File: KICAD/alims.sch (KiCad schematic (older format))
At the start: 20 parts

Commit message: minor cleanup
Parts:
- gave numbers to parts that had none: 2
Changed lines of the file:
@@
 $Descr A4 11693 8268
 encoding utf-8
-Sheet 13 16
+Sheet 16 16
 Title "SESAME"
 Date ""
@@
 $EndComp
 $Comp
-L Sesame:LT8365 U?
+L Sesame:LT8365 U14
 U 1 1 6123C49A
 P 4850 3400
-F 0 "U?" H 3650 3700 100 0000 L CNN
+F 0 "U14" H 3650 3700 100 0000 L CNN
 F 1 "LT8365" H 3500 3550 100 0000 L CNN
 F 2 "" H 4850 4100 100 0001 C CNN
@@
 AR Path="/60F171CE/6161C7FC" Ref="U?"  Part="3"
 AR Path="/60F19D5B/6161C7FC" Ref="U?"  Part="3"
-AR Path="/60F1AA92/6161C7FC" Ref="U?"  Part="3"
-F 0 "U?" H 963 6904 50  0000 R CNN
+AR Path="/60F1AA92/6161C7FC" Ref="U15"  Part="3"
+F 0 "U15" H 963 6904 50  0000 R CNN
 F 1 "AD8030" H 963 6995 50  0000 R CNN
 F 2 "Package_SO:SO-8_3.9x4.9mm_P1.27mm" H 1150 6950 50  0001 C CNN
@@
 $EndComp
 $Comp
-L Sesame:AD8030 U?
+L Sesame:AD8030 U15
 U 2 1 61592FA9
 P 10200 4550
-F 0 "U?" H 10200 4917 50  0000 C CNN
+F 0 "U15" H 10200 4917 50  0000 C CNN
 F 1 "AD8030" H 10200 4826 50  0000 C CNN
 F 2 "Package_SO:SO-8_3.9x4.9mm_P1.27mm" H 10200 4550 50  0001 C CNN
@@
 $EndComp
 $Comp
-L Sesame:AD8030 U?
+L Sesame:AD8030 U15
 U 1 1 615918A8
 P 9050 2900
-F 0 "U?" H 9050 3267 50  0000 C CNN
+F 0 "U15" H 9050 3267 50  0000 C CNN
 F 1 "AD8030" H 9050 3176 50  0000 C CNN
 F 2 "Package_SO:SO-8_3.9x4.9mm_P1.27mm" H 9050 2900 50  0001 C CNN

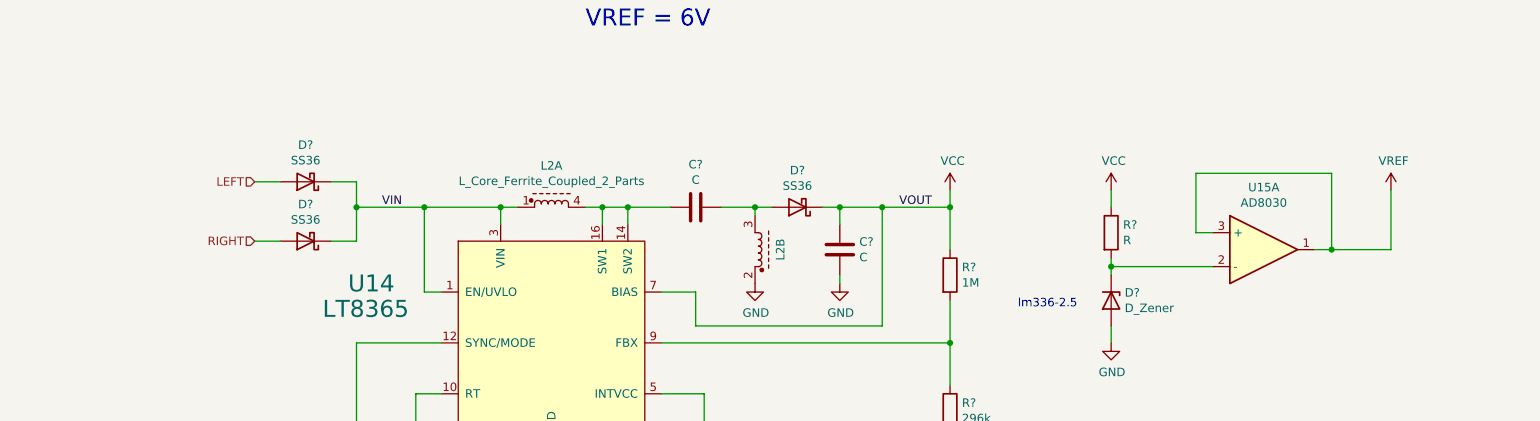
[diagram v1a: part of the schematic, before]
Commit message: drivers draft + clean and minors changes
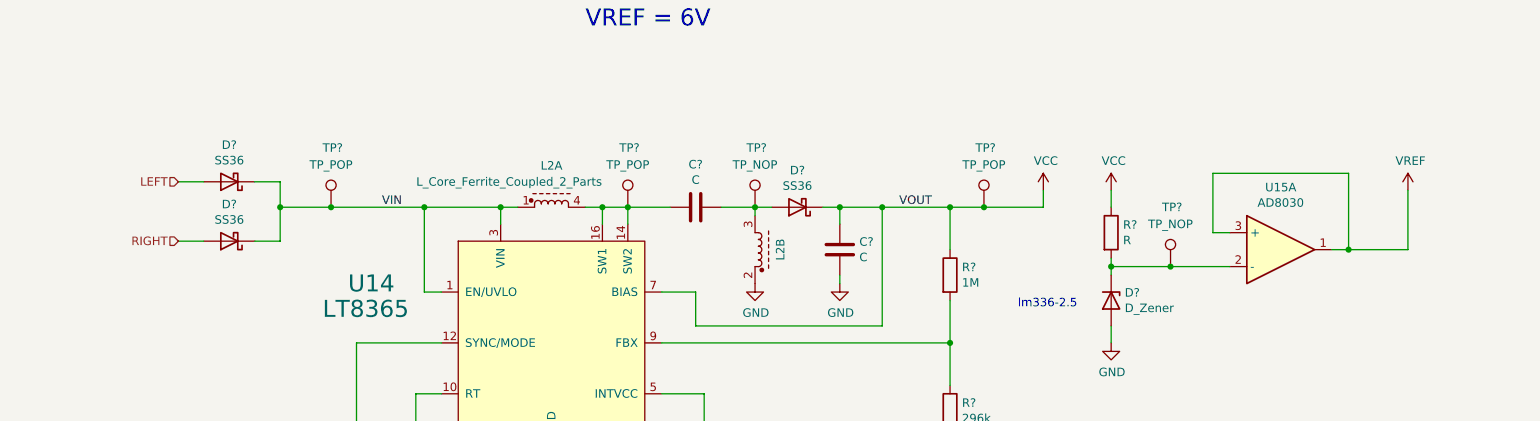
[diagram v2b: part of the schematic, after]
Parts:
- added TP? (x3): TP_POP, symbol Connector:TestPoint
- added TP? (x2): TP_NOP, symbol Connector:TestPoint
- R? (x3): footprint (none) -> Resistor_SMD:R_0805_2012Metric_Pad1.15x1.40mm_HandSolder
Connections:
- net VCC: now also TP?.1
- net VIN: now also TP?.1
- net at D?.1 (K), R?.2, U15.2 (-): now also TP?.1
- net at C?.2, L2.4 (3), U14.14 (SW2)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: now also TP?.1
- net at C?.1, D?.2 (A), L2.3: now also TP?.1
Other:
- moved on the sheet: D?, U15A
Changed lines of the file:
@@
 Comment4 ""
 $EndDescr
-Text HLabel 3100 2500 0    50   Input ~ 0
+Text HLabel 2650 2500 0    50   Input ~ 0
 LEFT
-Text HLabel 3100 2850 0    50   Input ~ 0
+Text HLabel 2650 2850 0    50   Input ~ 0
 RIGHT
 Wire Wire Line
-	8750 2800 8650 2800
-Wire Wire Line
-	9450 2900 9350 2900
+	8850 2800 8750 2800
+Wire Wire Line
+	9550 2900 9450 2900
 $Comp
 L power:GND #PWR0106
@@
 	8150 2950 8150 3000
 Wire Wire Line
-	8150 3000 8750 3000
+	8150 3000 8500 3000
 Connection ~ 8150 3000
 Wire Wire Line
 	8150 3000 8150 3050
 Wire Wire Line
+	2650 2850 2800 2850
+Wire Wire Line
+	2800 2500 2650 2500
+Wire Wire Line
+	3250 2850 3250 2650
+Wire Wire Line
 	3100 2850 3250 2850
 Wire Wire Line
-	3250 2500 3100 2500
-Wire Wire Line
-	3700 2850 3700 2650
-Wire Wire Line
-	3550 2850 3700 2850
-Wire Wire Line
-	3550 2500 3700 2500
+	3100 2500 3250 2500
 $Comp
 L Device:R R?
@@
 $EndComp
 Wire Wire Line
-	8650 2450 9450 2450
-Wire Wire Line
-	8650 2450 8650 2800
-Wire Wire Line
-	9450 2450 9450 2900
+	8750 2450 9550 2450
+Wire Wire Line
+	8750 2450 8750 2800
+Wire Wire Line
+	9550 2450 9550 2900
 $Comp
 L power:VCC #PWR0178
@@
 P 4850 2650
 F 0 "L2" H 4850 2895 50  0000 C CNN
-F 1 "L_Core_Ferrite_Coupled_2_Parts" H 4850 2804 50  0000 C CNN
+F 1 "L_Core_Ferrite_Coupled_2_Parts" H 4600 2800 50  0000 C CNN
 F 2 "" H 4850 2750 50  0001 C CNN
 F 3 "~" H 4850 2750 50  0001 C CNN
@@
 F 0 "R?" H 7270 3096 50  0000 L CNN
 F 1 "1M" H 7270 3005 50  0000 L CNN
-F 2 "" V 7130 3050 50  0001 C CNN
+F 2 "Resistor_SMD:R_0805_2012Metric_Pad1.15x1.40mm_HandSolder" V 7130 3050 50  0001 C CNN
 F 3 "~" H 7200 3050 50  0001 C CNN
 	1    7200 3050
@@
 F 0 "R?" H 7270 3896 50  0000 L CNN
 F 1 "296k" H 7270 3805 50  0000 L CNN
-F 2 "" V 7130 3850 50  0001 C CNN
+F 2 "Resistor_SMD:R_0805_2012Metric_Pad1.15x1.40mm_HandSolder" V 7130 3850 50  0001 C CNN
 F 3 "~" H 7200 3850 50  0001 C CNN
 	1    7200 3850
@@
 F 0 "R?" H 4120 4546 50  0000 L CNN
 F 1 "84.5" H 4120 4455 50  0000 L CNN
-F 2 "" V 3980 4500 50  0001 C CNN
+F 2 "Resistor_SMD:R_0805_2012Metric_Pad1.15x1.40mm_HandSolder" V 3980 4500 50  0001 C CNN
 F 3 "~" H 4050 4500 50  0001 C CNN
 	1    4050 4500
@@
 	5750 4850 5750 4650
 Wire Wire Line
-	4100 2650 3700 2650
+	4100 2650 3550 2650
 Connection ~ 4100 2650
-Connection ~ 3700 2650
-Wire Wire Line
-	3700 2650 3700 2500
+Connection ~ 3250 2650
+Wire Wire Line
+	3250 2650 3250 2500
 Text Label 3850 2650 0    50   ~ 0
 VIN
@@
 L Device:D_Schottky D?
 U 1 1 612B6943
-P 3400 2500
-F 0 "D?" H 3400 2283 50  0000 C CNN
-F 1 "SS36" H 3400 2374 50  0000 C CNN
-F 2 "Diode_SMD:D_SMA_Handsoldering" H 3400 2500 50  0001 C CNN
-F 3 "~" H 3400 2500 50  0001 C CNN
-	1    3400 2500
+P 2950 2500
+F 0 "D?" H 2950 2283 50  0000 C CNN
+F 1 "SS36" H 2950 2374 50  0000 C CNN
+F 2 "Diode_SMD:D_SMA_Handsoldering" H 2950 2500 50  0001 C CNN
+F 3 "~" H 2950 2500 50  0001 C CNN
+	1    2950 2500
 	-1   0    0    1
 $EndComp
@@
 L Device:D_Schottky D?
 U 1 1 612B7084
-P 3400 2850
-F 0 "D?" H 3400 2633 50  0000 C CNN
-F 1 "SS36" H 3400 2724 50  0000 C CNN
-F 2 "Diode_SMD:D_SMA_Handsoldering" H 3400 2850 50  0001 C CNN
-F 3 "~" H 3400 2850 50  0001 C CNN
-	1    3400 2850
+P 2950 2850
+F 0 "D?" H 2950 2633 50  0000 C CNN
+F 1 "SS36" H 2950 2724 50  0000 C CNN
+F 2 "Diode_SMD:D_SMA_Handsoldering" H 2950 2850 50  0001 C CNN
+F 3 "~" H 2950 2850 50  0001 C CNN
+	1    2950 2850
 	-1   0    0    1
 $EndComp
@@
 L power:VCC #PWR?
 U 1 1 612BD8C1
-P 7200 2550
-F 0 "#PWR?" H 7200 2400 50  0001 C CNN
-F 1 "VCC" H 7215 2723 50  0000 C CNN
-F 2 "" H 7200 2550 50  0001 C CNN
-F 3 "" H 7200 2550 50  0001 C CNN
-	1    7200 2550
-	1    0    0    -1
-$EndComp
-Wire Wire Line
-	7200 2550 7200 2650
+P 7750 2550
+F 0 "#PWR?" H 7750 2400 50  0001 C CNN
+F 1 "VCC" H 7765 2723 50  0000 C CNN
+F 2 "" H 7750 2550 50  0001 C CNN
+F 3 "" H 7750 2550 50  0001 C CNN
+	1    7750 2550
+	1    0    0    -1
+$EndComp
 Connection ~ 7200 2650
 $Comp
 L Sesame:VREF #PWR?
 U 1 1 612C58B4
-P 9800 2550
-F 0 "#PWR?" H 9800 2400 50  0001 C CNN
-F 1 "VREF" H 9815 2723 50  0000 C CNN
-F 2 "" H 9800 2550 50  0001 C CNN
-F 3 "" H 9800 2550 50  0001 C CNN
-	1    9800 2550
-	1    0    0    -1
-$EndComp
-Wire Wire Line
-	9800 2550 9800 2900
-Wire Wire Line
-	9800 2900 9450 2900
-Connection ~ 9450 2900
+P 9900 2550
+F 0 "#PWR?" H 9900 2400 50  0001 C CNN
+F 1 "VREF" H 9915 2723 50  0000 C CNN
+F 2 "" H 9900 2550 50  0001 C CNN
+F 3 "" H 9900 2550 50  0001 C CNN
+	1    9900 2550
+	1    0    0    -1
+$EndComp
+Wire Wire Line
+	9900 2550 9900 2900
+Wire Wire Line
+	9900 2900 9550 2900
+Connection ~ 9550 2900
 Text Notes 5050 1600 0    100  ~ 0
 VCC = 7V\nVREF = 6V
@@
 L Sesame:AD8030 U15
 U 1 1 615918A8
-P 9050 2900
-F 0 "U15" H 9050 3267 50  0000 C CNN
-F 1 "AD8030" H 9050 3176 50  0000 C CNN
-F 2 "Package_SO:SO-8_3.9x4.9mm_P1.27mm" H 9050 2900 50  0001 C CNN
-F 3 "~" H 9050 2900 50  0001 C CNN
-	1    9050 2900
-	1    0    0    -1
-$EndComp
+P 9150 2900
+F 0 "U15" H 9150 3267 50  0000 C CNN
+F 1 "AD8030" H 9150 3176 50  0000 C CNN
+F 2 "Package_SO:SO-8_3.9x4.9mm_P1.27mm" H 9150 2900 50  0001 C CNN
+F 3 "~" H 9150 2900 50  0001 C CNN
+	1    9150 2900
+	1    0    0    -1
+$EndComp
+$Comp
+L Connector:TestPoint TP?
+U 1 1 61513B8D
+P 3550 2650
+AR Path="/614794AE/61513B8D" Ref="TP?"  Part="1"
+AR Path="/61456C6A/61513B8D" Ref="TP?"  Part="1"
+AR Path="/61513B8D" Ref="TP?"  Part="1"
+AR Path="/60F1AA92/61513B8D" Ref="TP?"  Part="1"
+F 0 "TP?" H 3500 3000 50  0000 L CNN
+F 1 "TP_POP" H 3550 2900 50  0000 C CNN
+F 2 "" H 3750 2650 50  0001 C CNN
+F 3 "~" H 3750 2650 50  0001 C CNN
+	1    3550 2650
+	1    0    0    -1
+$EndComp
+Connection ~ 3550 2650
+Wire Wire Line
+	3550 2650 3250 2650
+$Comp
+L Connector:TestPoint TP?
+U 1 1 61522F2C
+P 7400 2650
+AR Path="/614794AE/61522F2C" Ref="TP?"  Part="1"
+AR Path="/61456C6A/61522F2C" Ref="TP?"  Part="1"
+AR Path="/61522F2C" Ref="TP?"  Part="1"
+AR Path="/60F1AA92/61522F2C" Ref="TP?"  Part="1"
+F 0 "TP?" H 7350 3000 50  0000 L CNN
+F 1 "TP_POP" H 7400 2900 50  0000 C CNN
+F 2 "" H 7600 2650 50  0001 C CNN
+F 3 "~" H 7600 2650 50  0001 C CNN
+	1    7400 2650
+	1    0    0    -1
+$EndComp
+Wire Wire Line
+	7400 2650 7200 2650
+Wire Wire Line
+	7750 2550 7750 2650
+Wire Wire Line
+	7750 2650 7400 2650
+Connection ~ 7400 2650
+$Comp
+L Connector:TestPoint TP?
+U 1 1 61530DA6
+P 5300 2650
+AR Path="/614794AE/61530DA6" Ref="TP?"  Part="1"
+AR Path="/61456C6A/61530DA6" Ref="TP?"  Part="1"
+AR Path="/61530DA6" Ref="TP?"  Part="1"
+AR Path="/60F1AA92/61530DA6" Ref="TP?"  Part="1"
+F 0 "TP?" H 5250 3000 50  0000 L CNN
+F 1 "TP_POP" H 5300 2900 50  0000 C CNN
+F 2 "" H 5500 2650 50  0001 C CNN
+F 3 "~" H 5500 2650 50  0001 C CNN
+	1    5300 2650
+	1    0    0    -1
+$EndComp
+$Comp
+L Connector:TestPoint TP?
+U 1 1 61533C44
+P 6050 2650
+AR Path="/614794AE/61533C44" Ref="TP?"  Part="1"
+AR Path="/61456C6A/61533C44" Ref="TP?"  Part="1"
+AR Path="/61533C44" Ref="TP?"  Part="1"
+AR Path="/60F1AA92/61533C44" Ref="TP?"  Part="1"
+F 0 "TP?" H 6000 3000 50  0000 L CNN
+F 1 "TP_NOP" H 6050 2900 50  0000 C CNN
+F 2 "" H 6250 2650 50  0001 C CNN
+F 3 "~" H 6250 2650 50  0001 C CNN
+	1    6050 2650
+	1    0    0    -1
+$EndComp
+$Comp
+L Connector:TestPoint TP?
+U 1 1 61535A79
+P 8500 3000
+AR Path="/614794AE/61535A79" Ref="TP?"  Part="1"
+AR Path="/61456C6A/61535A79" Ref="TP?"  Part="1"
+AR Path="/61535A79" Ref="TP?"  Part="1"
+AR Path="/60F1AA92/61535A79" Ref="TP?"  Part="1"
+F 0 "TP?" H 8450 3350 50  0000 L CNN
+F 1 "TP_NOP" H 8500 3250 50  0000 C CNN
+F 2 "" H 8700 3000 50  0001 C CNN
+F 3 "~" H 8700 3000 50  0001 C CNN
+	1    8500 3000
+	1    0    0    -1
+$EndComp
+Connection ~ 8500 3000
+Wire Wire Line
+	8500 3000 8850 3000
 $EndSCHEMATC

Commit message: review w/ jmt
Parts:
- removed D?: D_Zener, symbol Device:D_Zener
- added JP15, JP16: Jumper_2_Bridged, Jumper:SolderJumper-2_P1.3mm_Bridged_Pad1.0x1.5mm, symbol Jumper:Jumper_2_Bridged
- added R84: 10k, symbol Device:R
- added RV4: 10K, Potentiometer_SMD:Potentiometer_Bourns_3214W_Vertical, symbol Device:R_POT
- added TP44: TP_NOP, symbol Connector:TestPoint
- added U16: LM4040DBZ-2.5, Package_TO_SOT_SMD:SOT-23, symbol Reference_Voltage:LM4040DBZ-2.5
- R79, R81, R82: renamed from R?; footprint Resistor_SMD:R_0805_2012Metric_Pad1.15x1.40mm_HandSolder -> (none)
- U14: renamed from U15; footprint Package_SO:SO-8_3.9x4.9mm_P1.27mm -> (none)
- gave numbers to parts that had none: 16
- renumbered L2 to L1, U14 to U15
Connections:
- net GND: now also RV4.3, U16.2 (A)
- net VREF: now also JP15.1 (A), R84.1; no longer U14.3 (+), U14.5 (+)
- net at R83.2, TP43.1: now also U14.3 (+), U16.1 (K); no longer U14.2 (-)
- net at U14.6 (-): now also JP16.1 (A); no longer U14.7
- new net: R84.2, RV4.1, RV4.2, U14.2 (-)
- new net: JP15.2 (B), U14.5 (+)
- new net: JP16.2 (B), TP44.1, U14.7
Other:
- note added: "BOBINE !!!\nCondo serie"
- note added: "REF TENSION AUTRE SOLUTION\n"
- note removed: "lm336-2.5"
- moved on the sheet: D12, D13, R83, TP39, TP43, U14A, U14B

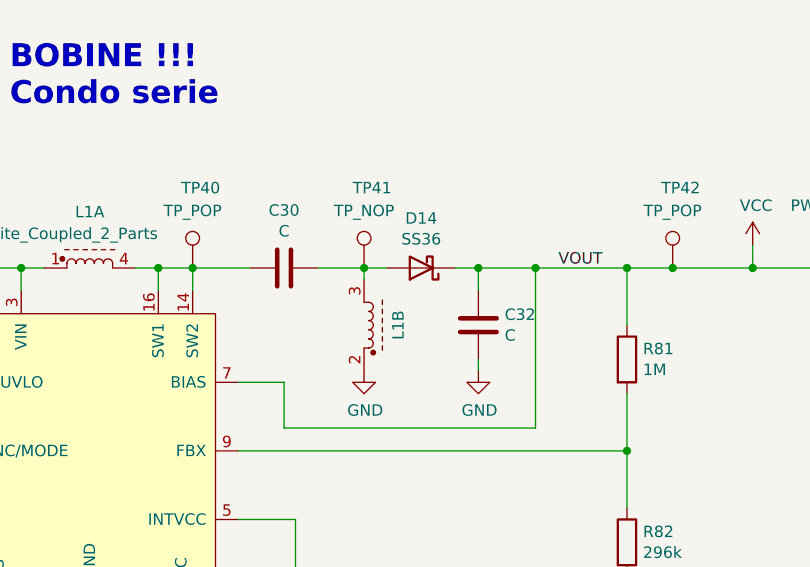
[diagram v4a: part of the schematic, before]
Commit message: edit footprints by jmt
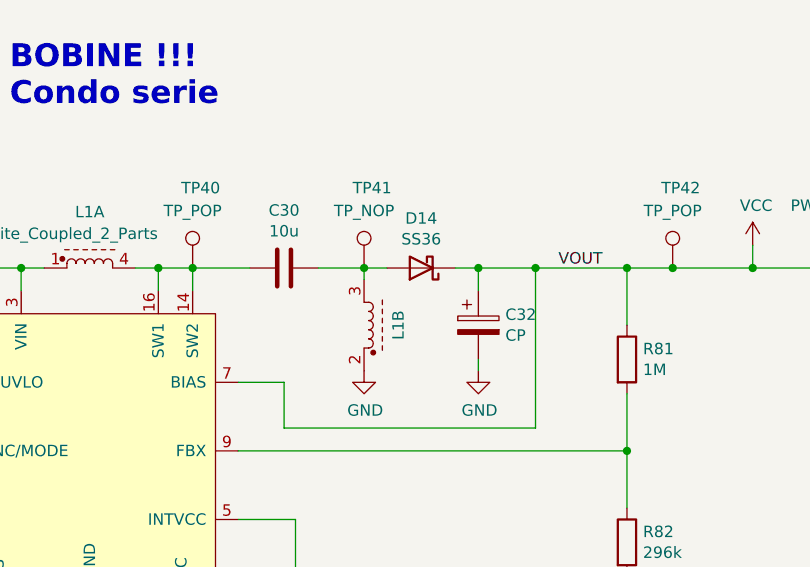
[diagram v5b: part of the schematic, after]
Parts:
- removed C32: C, symbol Device:C
- added C32: CP, symbol Device:CP
- C27, C28, C29, C31: footprint (none) -> Capacitor_SMD:C_0805_2012Metric_Pad1.15x1.40mm_HandSolder
- C30: value C -> 10u; footprint (none) -> Capacitor_SMD:C_1206_3216Metric_Pad1.42x1.75mm_HandSolder
- R79, R80, R81, R82, R83, R84: footprint (none) -> Resistor_SMD:R_0805_2012Metric_Pad1.15x1.40mm_HandSolder
- TP39, TP40, TP42: footprint (none) -> TestPoint:TestPoint_Loop_D1.80mm_Drill1.0mm_Beaded
- TP41, TP43, TP44: footprint (none) -> TestPoint:TestPoint_THTPad_D2.0mm_Drill1.0mm
- U14: footprint (none) -> Package_SO:SO-8_5.3x6.2mm_P1.27mm
- U15: footprint (none) -> Package_SO:MSOP-16-1EP_3x4mm_P0.5mm_EP1.65x2.85mm_ThermalVias
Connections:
- net GND: now also C32.2
- net VCC: now also C32.1
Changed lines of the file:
@@
 $Descr A4 11693 8268
 encoding utf-8
-Sheet 15 17
+Sheet 14 17
 Title "SESAME"
 Date ""
@@
 F 0 "R83" H 8870 2846 50  0000 L CNN
 F 1 "R" H 8870 2755 50  0000 L CNN
-F 2 "" V 8730 2800 50  0001 C CNN
+F 2 "Resistor_SMD:R_0805_2012Metric_Pad1.15x1.40mm_HandSolder" V 8730 2800 50  0001 C CNN
 F 3 "~" H 8800 2800 50  0001 C CNN
 	1    8800 2800
@@
 F 0 "U15" H 3650 3700 100 0000 L CNN
 F 1 "LT8365" H 3500 3550 100 0000 L CNN
-F 2 "" H 4850 4100 100 0001 C CNN
+F 2 "Package_SO:MSOP-16-1EP_3x4mm_P0.5mm_EP1.65x2.85mm_ThermalVias" H 4850 4100 100 0001 C CNN
 F 3 "" H 4850 4100 100 0001 C CNN
 	1    4850 3400
@@
 P 5700 2650
 F 0 "C30" V 5448 2650 50  0000 C CNN
-F 1 "C" V 5539 2650 50  0000 C CNN
-F 2 "" H 5738 2500 50  0001 C CNN
+F 1 "10u" V 5539 2650 50  0000 C CNN
+F 2 "Capacitor_SMD:C_1206_3216Metric_Pad1.42x1.75mm_HandSolder" H 5738 2500 50  0001 C CNN
 F 3 "~" H 5700 2650 50  0001 C CNN
 	1    5700 2650
@@
 F 0 "R80" H 5320 4396 50  0000 L CNN
 F 1 "R" H 5320 4305 50  0000 L CNN
-F 2 "" V 5180 4350 50  0001 C CNN
+F 2 "Resistor_SMD:R_0805_2012Metric_Pad1.15x1.40mm_HandSolder" V 5180 4350 50  0001 C CNN
 F 3 "~" H 5250 4350 50  0001 C CNN
 	1    5250 4350
@@
 Wire Wire Line
 	6550 2750 6550 2650
-$Comp
-L Device:C C32
-U 1 1 61257E1E
-P 6550 2900
-F 0 "C32" H 6435 2854 50  0000 R CNN
-F 1 "C" H 6435 2945 50  0000 R CNN
-F 2 "" H 6588 2750 50  0001 C CNN
-F 3 "~" H 6550 2900 50  0001 C CNN
-	1    6550 2900
-	-1   0    0    1
-$EndComp
 $Comp
 L power:GND #PWR0108
@@
 F 0 "R81" H 7270 3096 50  0000 L CNN
 F 1 "1M" H 7270 3005 50  0000 L CNN
-F 2 "" V 7130 3050 50  0001 C CNN
+F 2 "Resistor_SMD:R_0805_2012Metric_Pad1.15x1.40mm_HandSolder" V 7130 3050 50  0001 C CNN
 F 3 "~" H 7200 3050 50  0001 C CNN
 	1    7200 3050
@@
 F 0 "R82" H 7270 3896 50  0000 L CNN
 F 1 "296k" H 7270 3805 50  0000 L CNN
-F 2 "" V 7130 3850 50  0001 C CNN
+F 2 "Resistor_SMD:R_0805_2012Metric_Pad1.15x1.40mm_HandSolder" V 7130 3850 50  0001 C CNN
 F 3 "~" H 7200 3850 50  0001 C CNN
 	1    7200 3850
@@
 F 0 "C29" H 5365 4696 50  0000 L CNN
 F 1 "C" H 5365 4605 50  0000 L CNN
-F 2 "" H 5288 4500 50  0001 C CNN
+F 2 "Capacitor_SMD:C_0805_2012Metric_Pad1.15x1.40mm_HandSolder" H 5288 4500 50  0001 C CNN
 F 3 "~" H 5250 4650 50  0001 C CNN
 	1    5250 4650
@@
 F 0 "R79" H 4120 4546 50  0000 L CNN
 F 1 "84.5" H 4120 4455 50  0000 L CNN
-F 2 "" V 3980 4500 50  0001 C CNN
+F 2 "Resistor_SMD:R_0805_2012Metric_Pad1.15x1.40mm_HandSolder" V 3980 4500 50  0001 C CNN
 F 3 "~" H 4050 4500 50  0001 C CNN
 	1    4050 4500
@@
 F 0 "C28" H 4565 4546 50  0000 L CNN
 F 1 "C" H 4565 4455 50  0000 L CNN
-F 2 "" H 4488 4350 50  0001 C CNN
+F 2 "Capacitor_SMD:C_0805_2012Metric_Pad1.15x1.40mm_HandSolder" H 4488 4350 50  0001 C CNN
 F 3 "~" H 4450 4500 50  0001 C CNN
 	1    4450 4500
@@
 F 0 "C31" H 5865 4546 50  0000 L CNN
 F 1 "C" H 5865 4455 50  0000 L CNN
-F 2 "" H 5788 4350 50  0001 C CNN
+F 2 "Capacitor_SMD:C_0805_2012Metric_Pad1.15x1.40mm_HandSolder" H 5788 4350 50  0001 C CNN
 F 3 "~" H 5750 4500 50  0001 C CNN
 	1    5750 4500
@@
 F 0 "C27" H 1465 6996 50  0000 L CNN
 F 1 "100n" H 1465 6905 50  0000 L CNN
-F 2 "" H 1388 6800 50  0001 C CNN
+F 2 "Capacitor_SMD:C_0805_2012Metric_Pad1.15x1.40mm_HandSolder" H 1388 6800 50  0001 C CNN
 F 3 "~" H 1350 6950 50  0001 C CNN
 	1    1350 6950
@@
 F 0 "U14" H 963 6904 50  0000 R CNN
 F 1 "AD8030" H 963 6995 50  0000 R CNN
-F 2 "" H 1150 6950 50  0001 C CNN
+F 2 "Package_SO:SO-8_5.3x6.2mm_P1.27mm" H 1150 6950 50  0001 C CNN
 F 3 "~" H 1150 6950 50  0001 C CNN
 	3    1150 6950
@@
 F 0 "U14" H 9450 5817 50  0000 C CNN
 F 1 "AD8030" H 9450 5726 50  0000 C CNN
-F 2 "" H 9450 5450 50  0001 C CNN
+F 2 "Package_SO:SO-8_5.3x6.2mm_P1.27mm" H 9450 5450 50  0001 C CNN
 F 3 "~" H 9450 5450 50  0001 C CNN
 	2    9450 5450
@@
 F 0 "U14" H 10150 3467 50  0000 C CNN
 F 1 "AD8030" H 10150 3376 50  0000 C CNN
-F 2 "" H 10150 3100 50  0001 C CNN
+F 2 "Package_SO:SO-8_5.3x6.2mm_P1.27mm" H 10150 3100 50  0001 C CNN
 F 3 "~" H 10150 3100 50  0001 C CNN
 	1    10150 3100
@@
 F 0 "TP39" H 2900 3000 50  0000 L CNN
 F 1 "TP_POP" H 2950 2900 50  0000 C CNN
-F 2 "" H 3150 2650 50  0001 C CNN
+F 2 "TestPoint:TestPoint_Loop_D1.80mm_Drill1.0mm_Beaded" H 3150 2650 50  0001 C CNN
 F 3 "~" H 3150 2650 50  0001 C CNN
 	1    2950 2650
@@
 F 0 "TP42" H 7350 3000 50  0000 L CNN
 F 1 "TP_POP" H 7400 2900 50  0000 C CNN
-F 2 "" H 7600 2650 50  0001 C CNN
+F 2 "TestPoint:TestPoint_Loop_D1.80mm_Drill1.0mm_Beaded" H 7600 2650 50  0001 C CNN
 F 3 "~" H 7600 2650 50  0001 C CNN
 	1    7400 2650
@@
 F 0 "TP40" H 5250 3000 50  0000 L CNN
 F 1 "TP_POP" H 5300 2900 50  0000 C CNN
-F 2 "" H 5500 2650 50  0001 C CNN
+F 2 "TestPoint:TestPoint_Loop_D1.80mm_Drill1.0mm_Beaded" H 5500 2650 50  0001 C CNN
 F 3 "~" H 5500 2650 50  0001 C CNN
 	1    5300 2650
@@
 F 0 "TP41" H 6000 3000 50  0000 L CNN
 F 1 "TP_NOP" H 6050 2900 50  0000 C CNN
-F 2 "" H 6250 2650 50  0001 C CNN
+F 2 "TestPoint:TestPoint_THTPad_D2.0mm_Drill1.0mm" H 6250 2650 50  0001 C CNN
 F 3 "~" H 6250 2650 50  0001 C CNN
 	1    6050 2650
@@
 F 0 "TP43" H 9350 3350 50  0000 L CNN
 F 1 "TP_NOP" H 9400 3250 50  0000 C CNN
-F 2 "" H 9600 3000 50  0001 C CNN
+F 2 "TestPoint:TestPoint_THTPad_D2.0mm_Drill1.0mm" H 9600 3000 50  0001 C CNN
 F 3 "~" H 9600 3000 50  0001 C CNN
 	1    9400 3000
@@
 F 0 "R84" V 9943 3500 50  0000 C CNN
 F 1 "10k" V 10034 3500 50  0000 C CNN
-F 2 "" V 10080 3500 50  0001 C CNN
+F 2 "Resistor_SMD:R_0805_2012Metric_Pad1.15x1.40mm_HandSolder" V 10080 3500 50  0001 C CNN
 F 3 "~" H 10150 3500 50  0001 C CNN
 	1    10150 3500
@@
 F 0 "TP44" H 10000 5800 50  0000 L CNN
 F 1 "TP_NOP" H 10050 5700 50  0000 C CNN
-F 2 "" H 10250 5450 50  0001 C CNN
+F 2 "TestPoint:TestPoint_THTPad_D2.0mm_Drill1.0mm" H 10250 5450 50  0001 C CNN
 F 3 "~" H 10250 5450 50  0001 C CNN
 	1    10050 5450
@@
 Text Notes 8500 3350 0    100  ~ 20
 REF TENSION AUTRE SOLUTION\n
+$Comp
+L Device:CP C32
+U 1 1 6126F44E
+P 6550 2900
+F 0 "C32" H 6668 2946 50  0000 L CNN
+F 1 "CP" H 6668 2855 50  0000 L CNN
+F 2 "" H 6588 2750 50  0001 C CNN
+F 3 "~" H 6550 2900 50  0001 C CNN
+	1    6550 2900
+	1    0    0    -1
+$EndComp
 $EndSCHEMATC
